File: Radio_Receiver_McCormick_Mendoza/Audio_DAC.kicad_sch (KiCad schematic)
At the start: 28 parts, among them J35 3.5mm_Jack, J38 DAC_FLT, J40 DAC_FMT, U14 PCM5102A

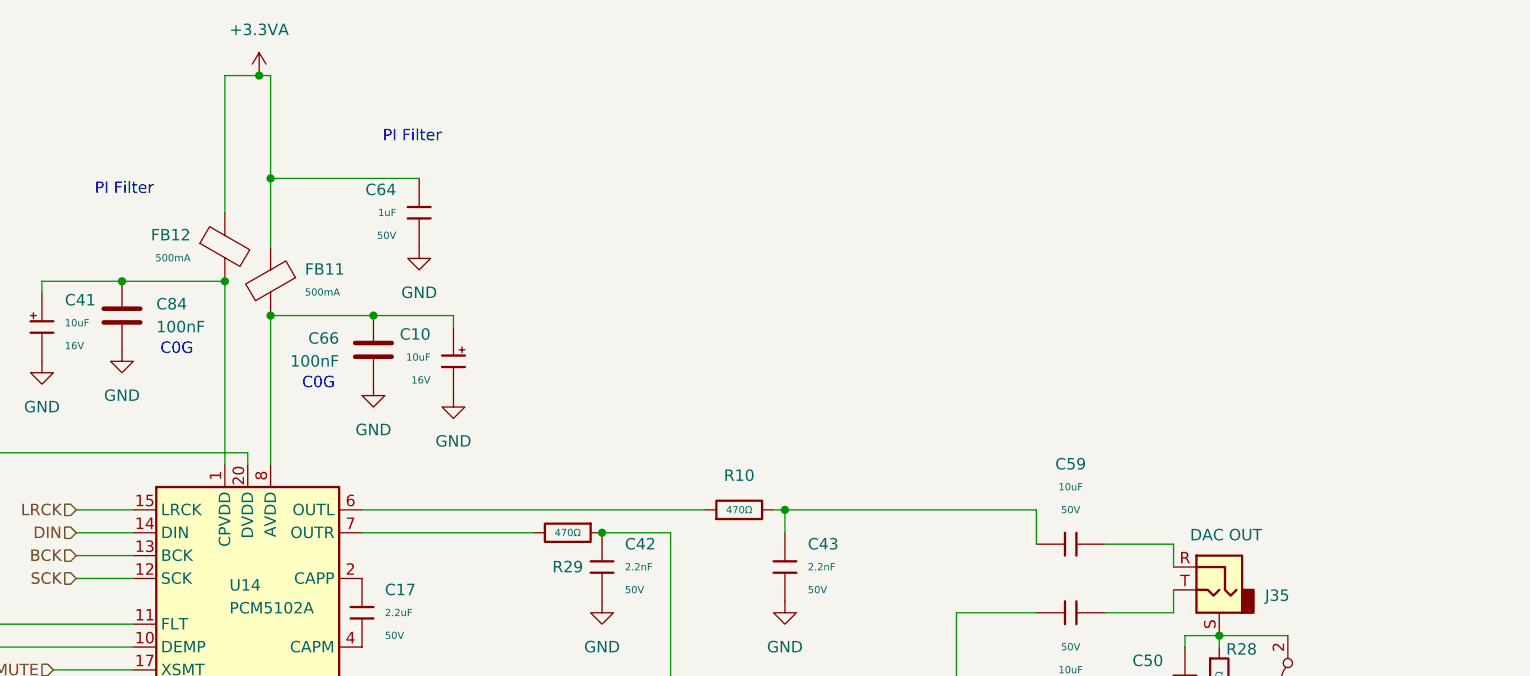
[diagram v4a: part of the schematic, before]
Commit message: Swapped voltage regulator to output 4.5V
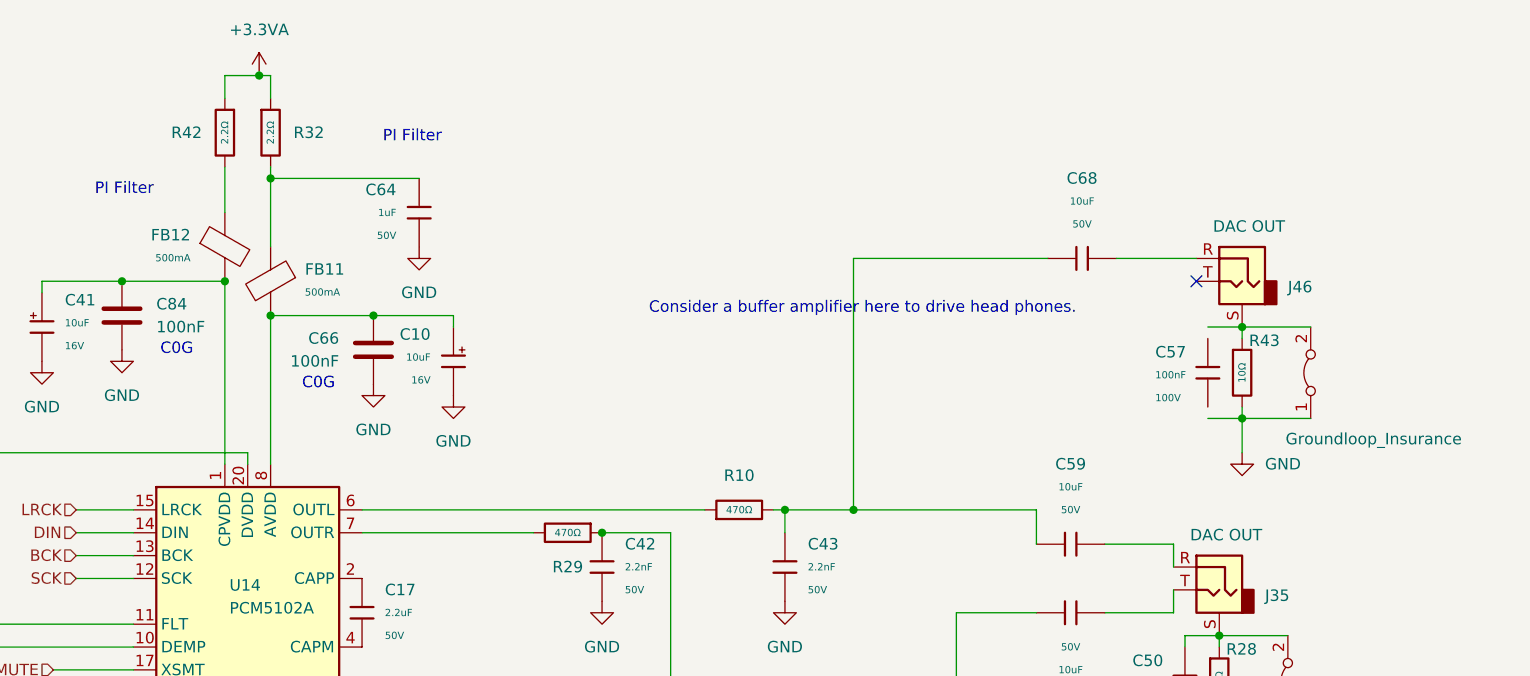
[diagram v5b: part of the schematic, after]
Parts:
- added C57: 100nF, PCM_JLCPCB:C_0805, symbol PCM_JLCPCB-Capacitors:0805,100nF
- added C68: 10uF, PCM_JLCPCB:C_0805, symbol PCM_JLCPCB-Capacitors:0805,10uF,(2)
- added J46: 3.5mm_Jack, Connector_Audio:Jack_3.5mm_CUI_SJ-3523-SMT_Horizontal, symbol Connector_Audio:AudioJack2_Ground
- added R32, R42: 2.2Ω, PCM_JLCPCB:R_0805, symbol PCM_JLCPCB-Resistors:0805,2.2Ω
- added R43: 10Ω, PCM_JLCPCB:R_0603, symbol PCM_JLCPCB-Resistors:0603,10Ω
- added e4: Groundloop_Insurance, Jumper:SolderJumper-2_P1.3mm_Bridged_RoundedPad1.0x1.5mm, symbol Jumper:Jumper_2_Bridged
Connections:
- net +3.3VA: now also R32.1, R42.1; no longer C64.1, FB11.1, FB12.1
- net GND: now also R43.2, e4.1 (A)
- net at C43.1, C59.1, R10.2: now also C68.1
- new net: C64.1, FB11.1, R32.2
- new net: C68.2, J46.R
- new net: J46.S, R43.1, e4.2 (B)
- new net: FB12.1, R42.2
- no-connect marks 0 -> 1
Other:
- note added: "Consider a buffer amplifier here to drive head phones."

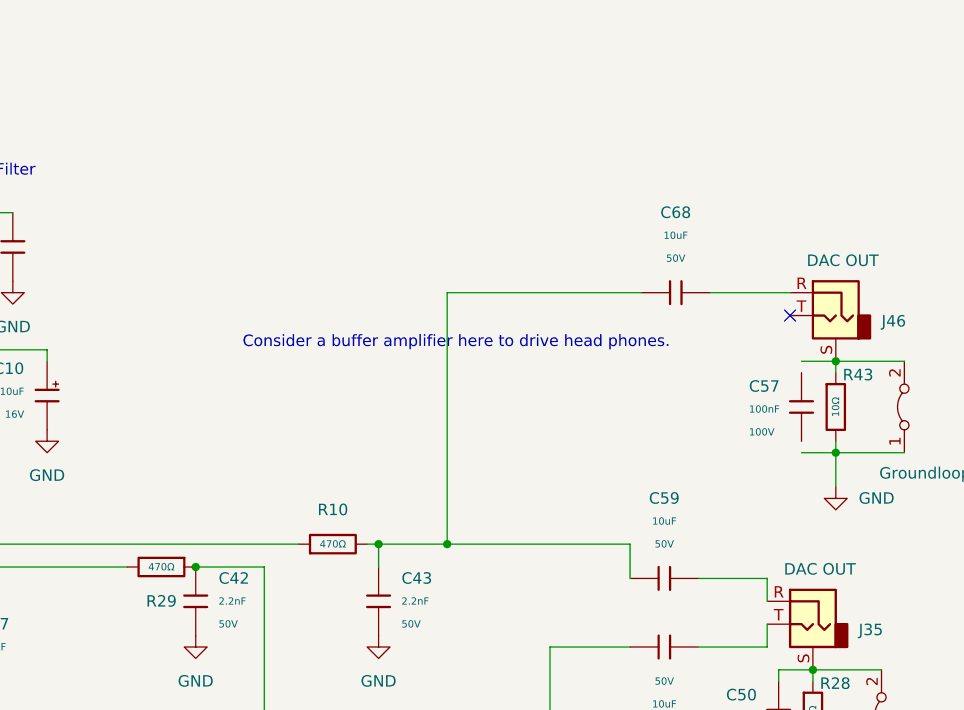
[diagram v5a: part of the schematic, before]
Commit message: Corrected mono to headphones
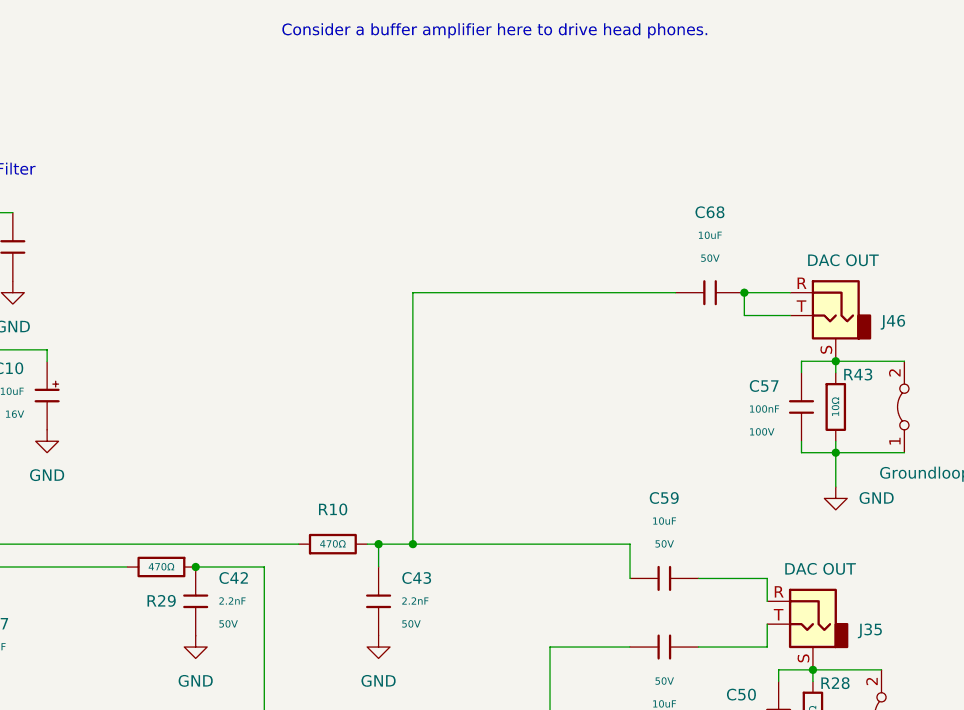
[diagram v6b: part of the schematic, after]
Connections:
- net GND: now also C57.1
- net at C68.2, J46.R: now also J46.T
- net at J46.S, R43.1, e4.2 (B): now also C57.2
- no-connect marks 1 -> 0
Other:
- moved on the sheet: C68
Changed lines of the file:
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@@
 	(text "Consider a buffer amplifier here to drive head phones."
 		(exclude_from_sim no)
-		(at 195.326 56.388 0)
+		(at 199.644 21.844 0)
 		(effects
 			(font
@@
 	)
 	(junction
-		(at 194.31 78.74)
-		(diameter 0)
-		(color 0 0 0 0)
-	)
-	(junction
 		(at 140.97 57.15)
 		(diameter 0)
@@
 	)
 	(junction
+		(at 190.5 78.74)
+		(diameter 0)
+		(color 0 0 0 0)
+	)
+	(junction
 		(at 234.95 102.87)
 		(diameter 0)
@@
 	)
 	(junction
+		(at 227.33 50.8)
+		(diameter 0)
+		(color 0 0 0 0)
+	)
+	(junction
 		(at 237.49 68.58)
 		(diameter 0)
@@
 		(color 0 0 0 0)
 	)
-	(no_connect
-		(at 232.41 53.34)
-	)
 	(wire
 		(pts
@@
 	(wire
 		(pts
-			(xy 194.31 50.8) (xy 194.31 78.74)
+			(xy 190.5 50.8) (xy 190.5 78.74)
+		)
+		(stroke
+			(width 0)
+			(type default)
+		)
+	)
+	(wire
+		(pts
+			(xy 227.33 50.8) (xy 227.33 53.34)
 		)
 		(stroke
@@
 	(wire
 		(pts
-			(xy 215.9 50.8) (xy 194.31 50.8)
+			(xy 219.71 50.8) (xy 190.5 50.8)
 		)
 		(stroke
@@
 	(wire
 		(pts
-			(xy 194.31 78.74) (xy 214.63 78.74)
-		)
-		(stroke
-			(width 0)
-			(type default)
-		)
-	)
-	(wire
-		(pts
 			(xy 76.2 57.15) (xy 85.09 57.15)
 		)
@@
 	(wire
 		(pts
-			(xy 232.41 50.8) (xy 223.52 50.8)
+			(xy 232.41 50.8) (xy 227.33 50.8)
+		)
+		(stroke
+			(width 0)
+			(type default)
+		)
+	)
+	(wire
+		(pts
+			(xy 227.33 53.34) (xy 232.41 53.34)
 		)
 		(stroke
@@
 	(wire
 		(pts
-			(xy 186.69 78.74) (xy 194.31 78.74)
+			(xy 186.69 78.74) (xy 190.5 78.74)
 		)
 		(stroke
@@
 	(wire
 		(pts
+			(xy 233.68 67.31) (xy 233.68 68.58)
+		)
+		(stroke
+			(width 0)
+			(type default)
+		)
+	)
+	(wire
+		(pts
 			(xy 222.25 82.55) (xy 229.87 82.55)
 		)
@@
 	(wire
 		(pts
+			(xy 233.68 58.42) (xy 233.68 59.69)
+		)
+		(stroke
+			(width 0)
+			(type default)
+		)
+	)
+	(wire
+		(pts
 			(xy 124.46 30.48) (xy 128.27 30.48)
 		)
@@
 	(wire
 		(pts
+			(xy 190.5 78.74) (xy 214.63 78.74)
+		)
+		(stroke
+			(width 0)
+			(type default)
+		)
+	)
+	(wire
+		(pts
 			(xy 167.64 124.46) (xy 156.21 124.46)
 		)
@@
 	(symbol
 		(lib_id "PCM_JLCPCB-Capacitors:0805,10uF,(2)")
-		(at 219.71 50.8 90)
+		(at 223.52 50.8 90)
 		(unit 1)
 		(body_style 1)
@@
 		(fields_autoplaced yes)
 		(property "Reference" "C68"
-			(at 219.71 41.91 90)
+			(at 223.52 41.91 90)
 			(show_name no)
 			(do_not_autoplace no)
@@
 		)
 		(property "Value" "10uF"
-			(at 219.71 44.45 90)
+			(at 223.52 44.45 90)
 			(show_name no)
 			(do_not_autoplace no)
@@
 		)
 		(property "Footprint" "PCM_JLCPCB:C_0805"
-			(at 219.71 52.578 90)
+			(at 223.52 52.578 90)
 			(hide yes)
 			(show_name no)
@@
 		)
 		(property "Datasheet" "https://www.lcsc.com/datasheet/lcsc_datasheet_2411041759_Murata-Electronics-GRM21BR61H106KE43L_C440198.pdf"
-			(at 219.71 50.8 0)
+			(at 223.52 50.8 0)
 			(hide yes)
 			(show_name no)
@@
 		)
 		(property "Description" "50V 10uF X5R ±10% 0805 Multilayer Ceramic Capacitors MLCC - SMD/SMT ROHS"
-			(at 219.71 50.8 0)
+			(at 223.52 50.8 0)
 			(hide yes)
 			(show_name no)
@@
 		)
 		(property "LCSC" "C440198"
-			(at 219.71 50.8 0)
+			(at 223.52 50.8 0)
 			(hide yes)
 			(show_name no)
@@
 		)
 		(property "Stock" "1422246"
-			(at 219.71 50.8 0)
+			(at 223.52 50.8 0)
 			(hide yes)
 			(show_name no)
@@
 		)
 		(property "Price" "0.066USD"
-			(at 219.71 50.8 0)
+			(at 223.52 50.8 0)
 			(hide yes)
 			(show_name no)
@@
 		)
 		(property "Process" "SMT"
-			(at 219.71 50.8 0)
+			(at 223.52 50.8 0)
 			(hide yes)
 			(show_name no)
@@
 		)
 		(property "Minimum Qty" "5"
-			(at 219.71 50.8 0)
+			(at 223.52 50.8 0)
 			(hide yes)
 			(show_name no)
@@
 		)
 		(property "Attrition Qty" "4"
-			(at 219.71 50.8 0)
+			(at 223.52 50.8 0)
 			(hide yes)
 			(show_name no)
@@
 		)
 		(property "Class" "Basic Component"
-			(at 219.71 50.8 0)
+			(at 223.52 50.8 0)
 			(hide yes)
 			(show_name no)
@@
 		)
 		(property "Category" "Capacitors,Multilayer Ceramic Capacitors MLCC - SMD/SMT"
-			(at 219.71 50.8 0)
+			(at 223.52 50.8 0)
 			(hide yes)
 			(show_name no)
@@
 		)
 		(property "Part" "GRM21BR61H106KE43L"
-			(at 219.71 50.8 0)
+			(at 223.52 50.8 0)
 			(hide yes)
 			(show_name no)
@@
 		)
 		(property "Voltage Rated" "50V"
-			(at 219.71 46.99 90)
+			(at 223.52 46.99 90)
 			(show_name no)
 			(do_not_autoplace no)
@@
 		)
 		(property "Tolerance" "±10%"
-			(at 219.71 50.8 0)
+			(at 223.52 50.8 0)
 			(hide yes)
 			(show_name no)
@@
 		)
 		(property "Capacitance" "10uF"
-			(at 219.71 50.8 0)
+			(at 223.52 50.8 0)
 			(hide yes)
 			(show_name no)
@@
 		)
 		(property "Temperature Coefficient" "X5R"
-			(at 219.71 50.8 0)
+			(at 223.52 50.8 0)
 			(hide yes)
 			(show_name no)

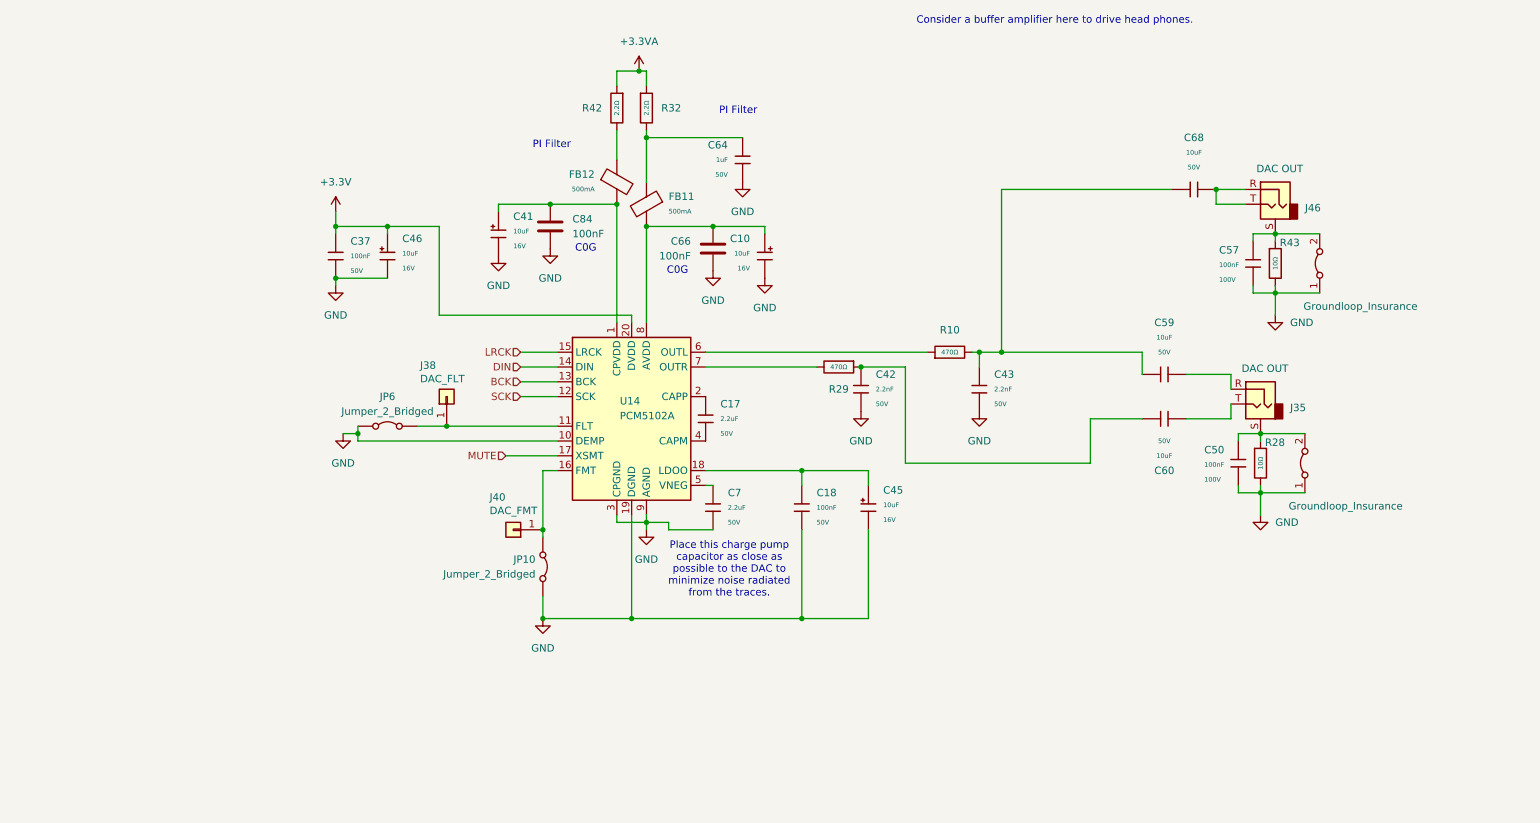
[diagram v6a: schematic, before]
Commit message: Created low mono, high stereo impedance DAC audio outlets
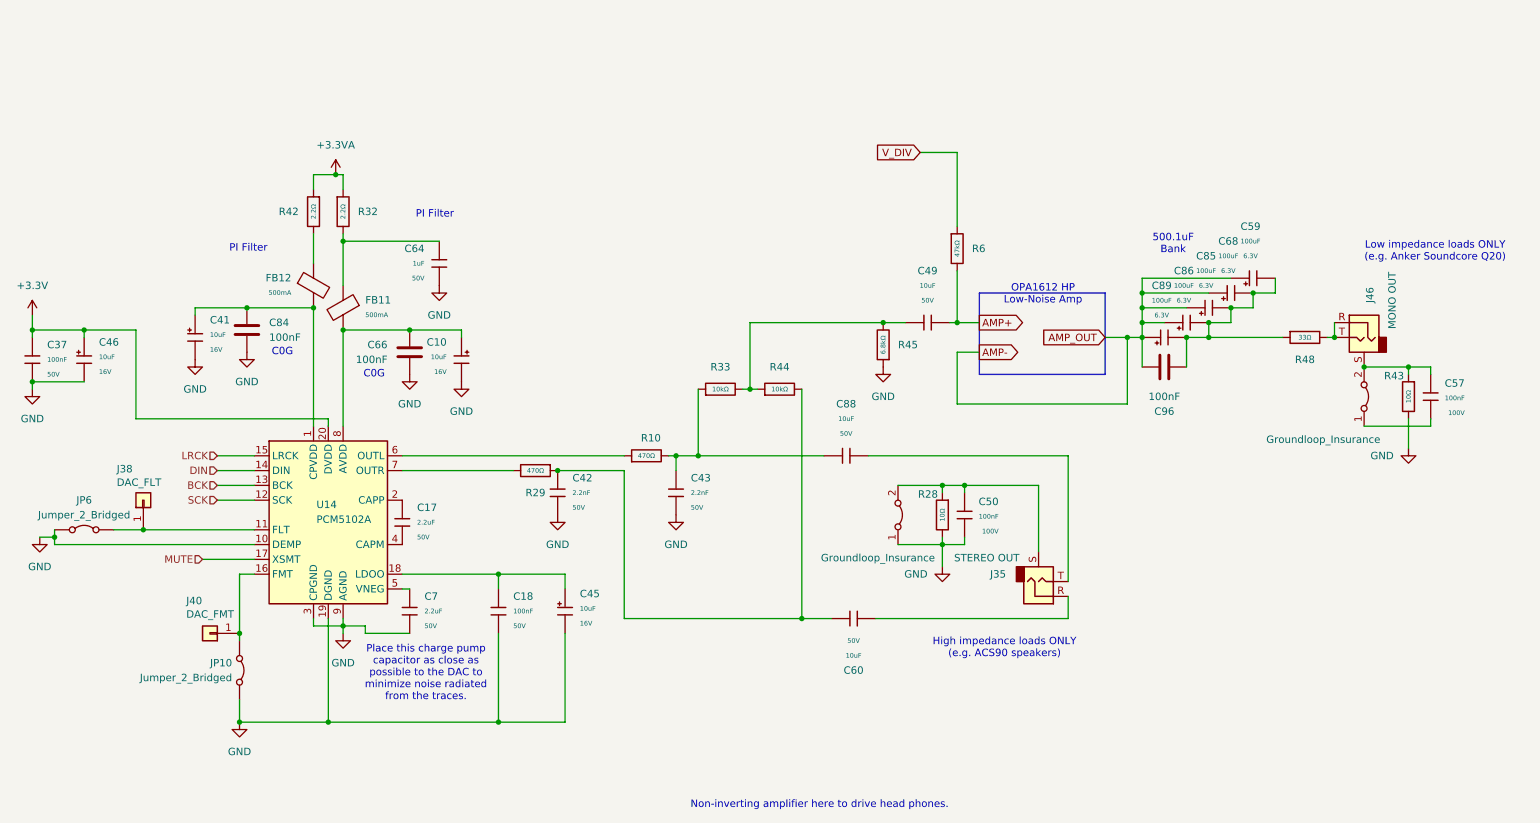
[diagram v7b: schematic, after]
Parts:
- removed C59, C68: 10uF, PCM_JLCPCB:C_0805, symbol PCM_JLCPCB-Capacitors:0805,10uF,(2)
- added C49, C88: 10uF, PCM_JLCPCB:C_0805, symbol PCM_JLCPCB-Capacitors:0805,10uF,(2)
- added C59, C68, C85, C86, C89: 100uF, PCM_JLCPCB:C_CASE-B-3528-21(mm), symbol PCM_JLCPCB-Capacitors:CASE-B-3528-21(mm),100uF
- added C96: 100nF, PCM_JLCPCB:C_1206, symbol Device:C
- added R33, R44: 10kΩ, PCM_JLCPCB:R_0805, symbol PCM_JLCPCB-Resistors:0805,10kΩ
- added R45: 6.8kΩ, PCM_JLCPCB:R_0603, symbol PCM_JLCPCB-Resistors:0603,6.8kΩ
- added R48: 33Ω, PCM_JLCPCB:R_0805, symbol PCM_JLCPCB-Resistors:0805,33Ω
- added R6: 47kΩ, PCM_JLCPCB:R_0603, symbol PCM_JLCPCB-Resistors:0603,47kΩ
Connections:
- net GND: now also R45.1; no longer C57.1, e4.1 (A)
- net at C42.1, C60.1, R29.1: now also R44.2
- net at C43.1, R10.2: now also C88.2, R33.1
- net at J35.R: now also C60.2
- net at J46.R, J46.T: now also R48.2
- net at J35.T: now also C88.1; no longer C60.2
- new net: C49.1, R33.2, R44.1, R45.2
- new net: C59.2, C68.2, C85.2, C86.2, C89.2, C96.2, R48.1
- new net: C57.1, e4.1 (A)
- new net AMP+: C49.2, R6.2
- new net AMP-: C59.1, C68.1, C85.1, C86.1, C89.1, C96.1
- new net V_DIV: R6.1
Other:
- note added: "500.1uF Bank"
- note added: "High impedance loads ONLY (e.g. ACS90 speakers)"
- note added: "Low impedance loads ONLY (e.g. Anker Soundcore Q20)"
- note added: "Non-inverting amplifier here to drive head phones."
- note added: "OPA1612 HP Low-Noise Amp"
- note removed: "Consider a buffer amplifier here to drive head phones."
- moved on the sheet: C10, C17, C18, C37, C41, C42, C43, C45, C46, C50, C57, C60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
